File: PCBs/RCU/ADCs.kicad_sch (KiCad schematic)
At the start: 12 parts, among them U600 MCP3021A5T-E/OT, U601 MCP3021A5T-E/OT, U601 OPA365xxD, U603 OPA365xxD

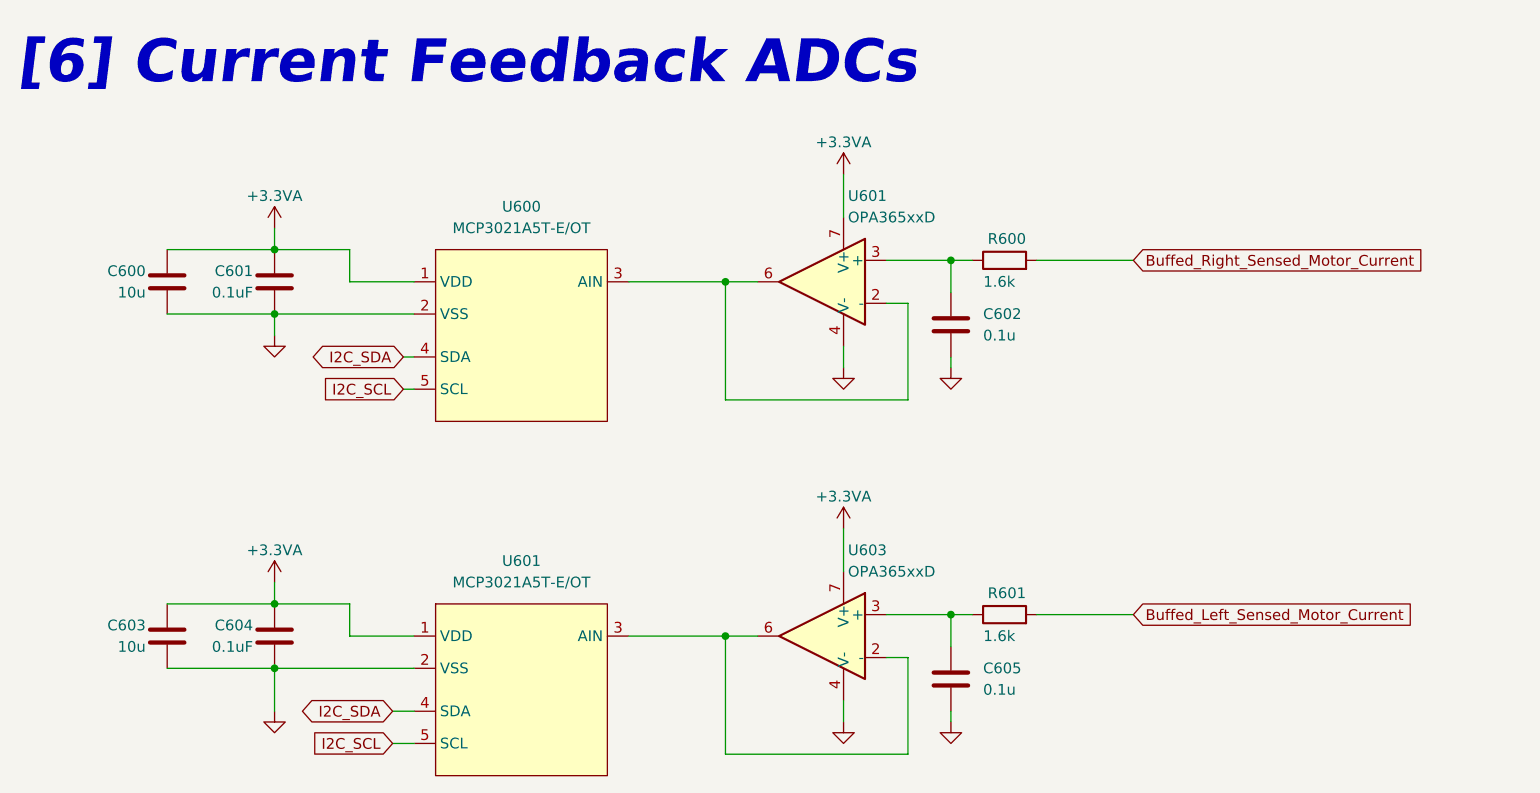
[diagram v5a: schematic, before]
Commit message: Sectioned ADC module and corrected Motor current output name
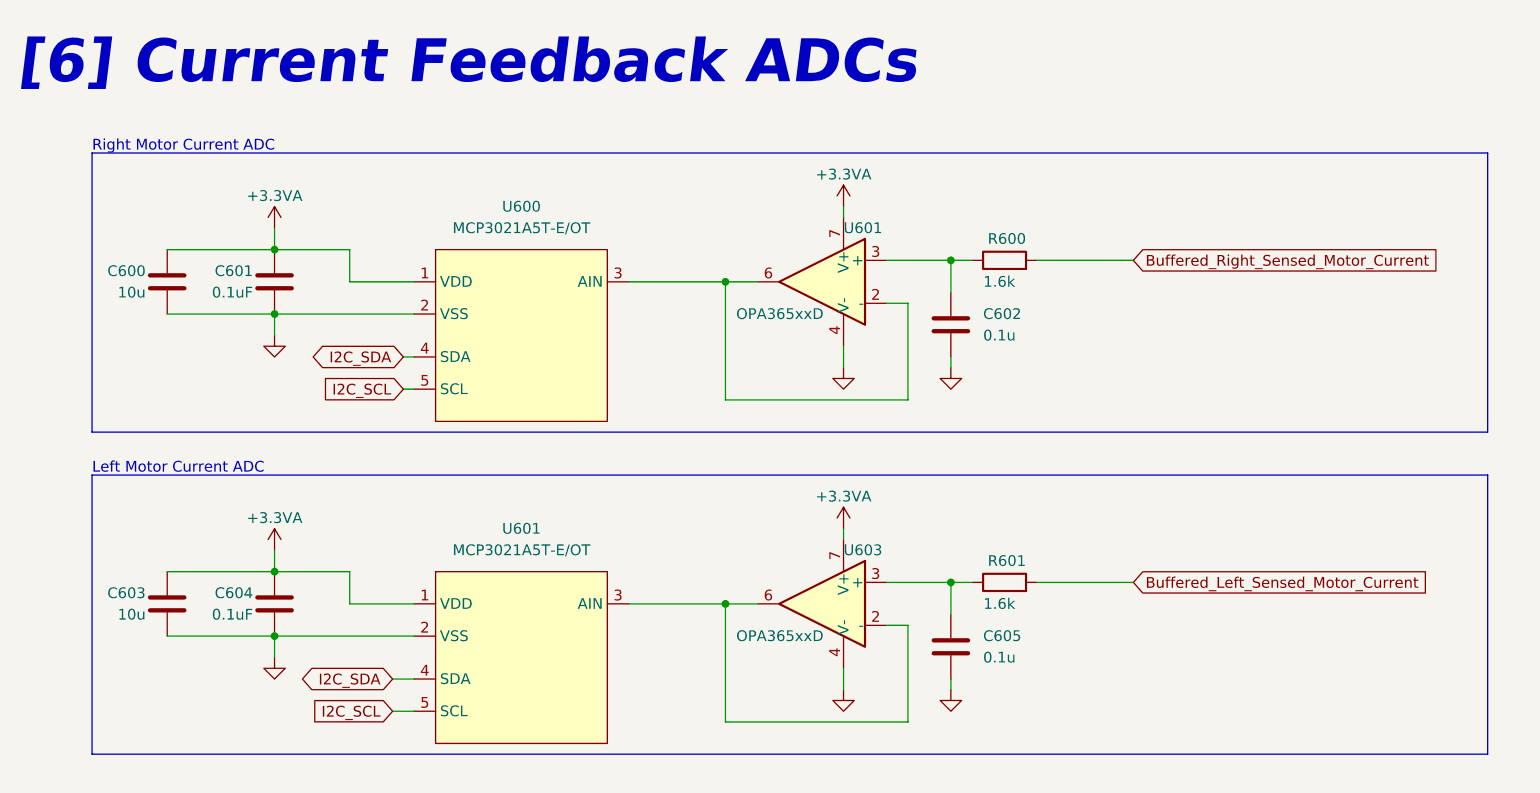
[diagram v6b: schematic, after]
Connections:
- net Buffed_Left_Sensed_Motor_Current renamed Buffered_Left_Sensed_Motor_Current
- net Buffed_Right_Sensed_Motor_Current renamed Buffered_Right_Sensed_Motor_Current
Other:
- note added: "Left Motor Current ADC"
- note added: "Right Motor Current ADC"
- moved on the sheet: C603, C604, C605, R601, U601, U603

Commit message: Replaced ADCs with ADC121C027, easy to program the addresses
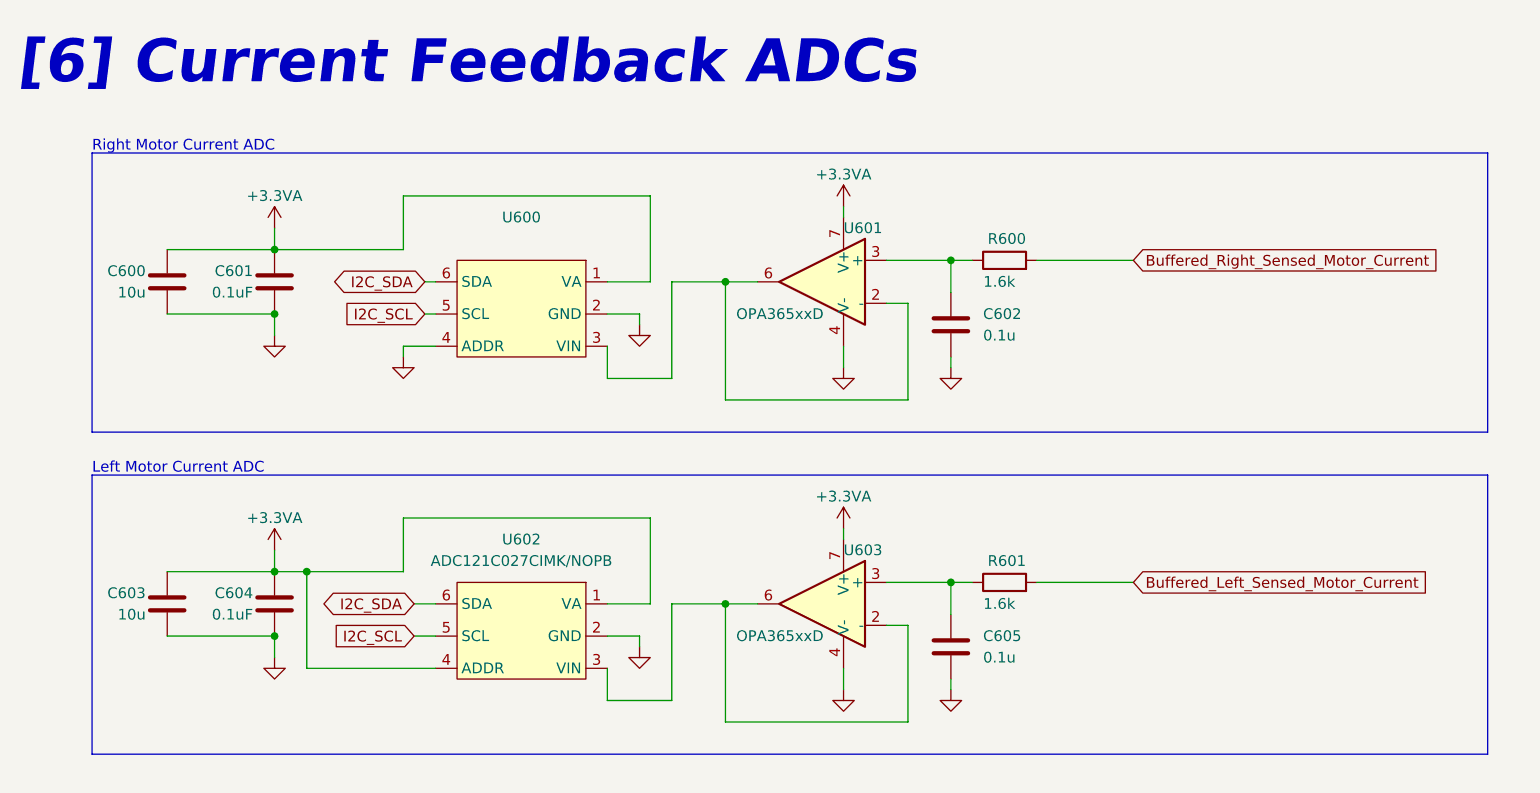
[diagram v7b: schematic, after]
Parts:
- removed U600, U601: MCP3021A5T-E/OT, symbol Ghanis_Symbols_KiCad6:MCP3021A5T-E/OT
- added U600: (no value), symbol Ghanis_Symbols_KiCad6:ADC121C027CIMK/NOPB
- added U602: ADC121C027CIMK/NOPB, symbol Ghanis_Symbols_KiCad6:ADC121C027CIMK/NOPB
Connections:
- net +3.3VA: now also U600.1 (VA), U602.1 (VA), U602.4 (ADDR)
- net GND: now also U600.2 (GND), U600.4 (ADDR), U602.2 (GND)
- net I2C_SCL: now also U600.5 (SCL), U602.5 (SCL)
- net I2C_SDA: now also U600.6 (SDA), U602.6 (SDA)
- net at U601.2 (-), U601.6: now also U600.3 (VIN)
- net at U603.2 (-), U603.6: now also U602.3 (VIN)

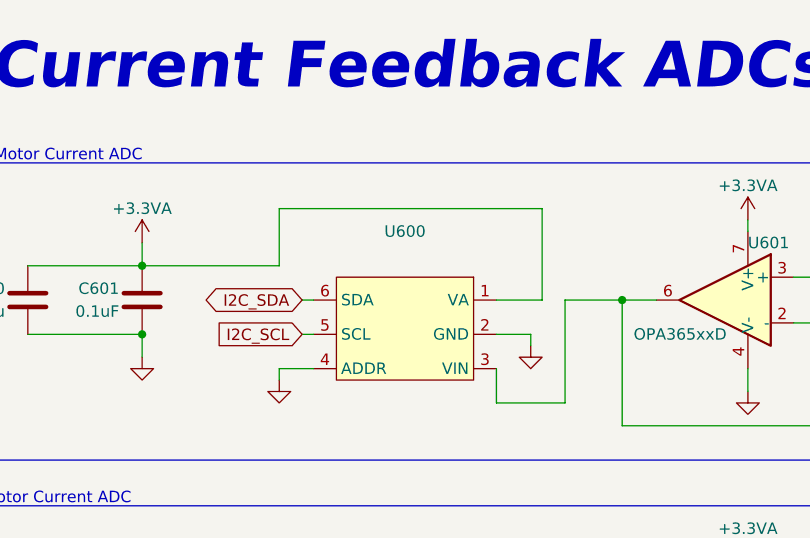
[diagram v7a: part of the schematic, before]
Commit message: Added 32Mbit external memory with SPI interface
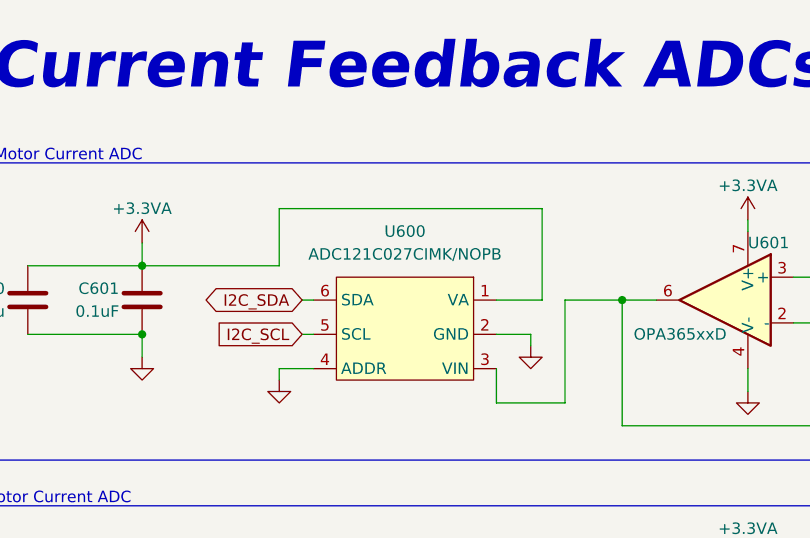
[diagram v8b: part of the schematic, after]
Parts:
- U600: value (none) -> ADC121C027CIMK/NOPB
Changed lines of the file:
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@@
     (in_bom yes) (on_board yes) (fields_autoplaced)
     (property "Reference" "U600" (id 0) (at 74.93 38.1 0))
-    (property "Value" "" (id 1) (at 74.93 40.64 0))
+    (property "Value" "ADC121C027CIMK/NOPB" (id 1) (at 74.93 40.64 0))
     (property "Footprint" "" (id 2) (at 85.09 39.37 0)
       (effects (font (size 1.27 1.27)) hide)
